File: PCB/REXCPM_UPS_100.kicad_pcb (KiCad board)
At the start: 2 copper layers, 51.3 x 18.3 mm, 14 parts, among them J1 Model_100_System_BUS, J2 SM04B, U1 2G02

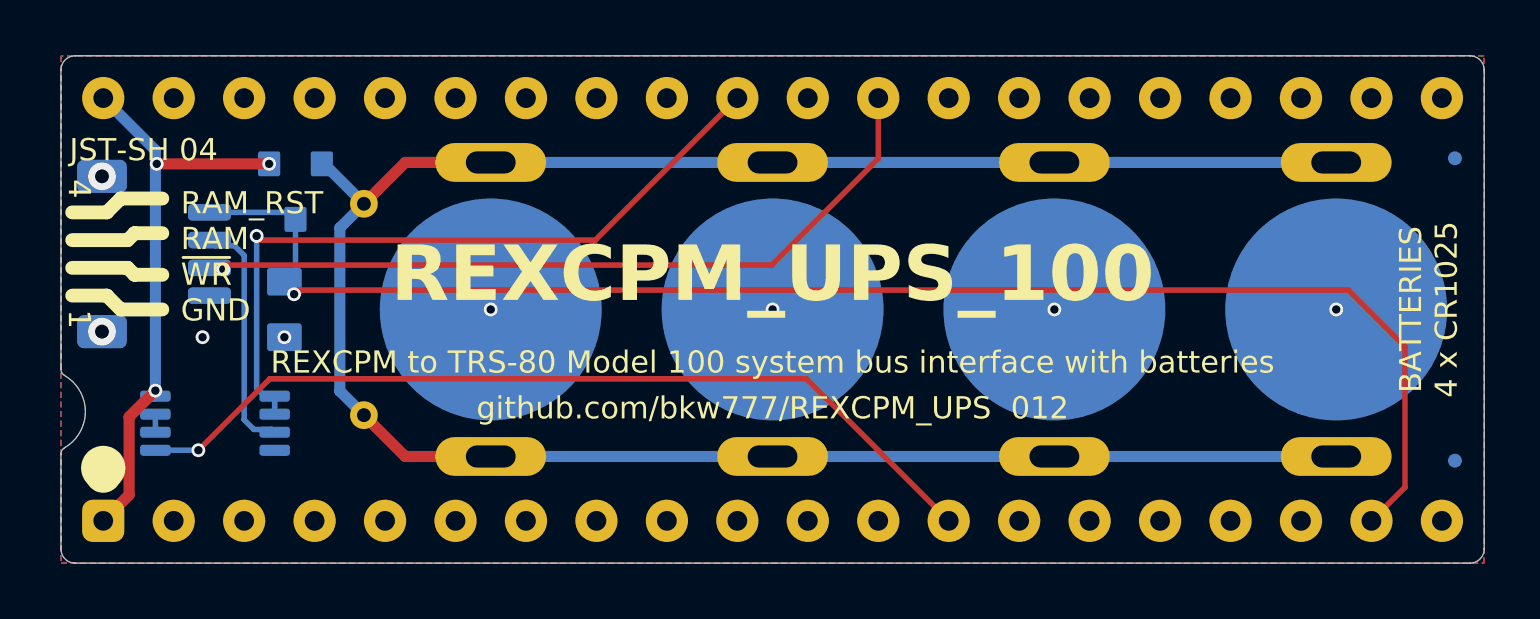
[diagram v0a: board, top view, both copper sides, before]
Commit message: move 1u cap from RAMRST to VBUS
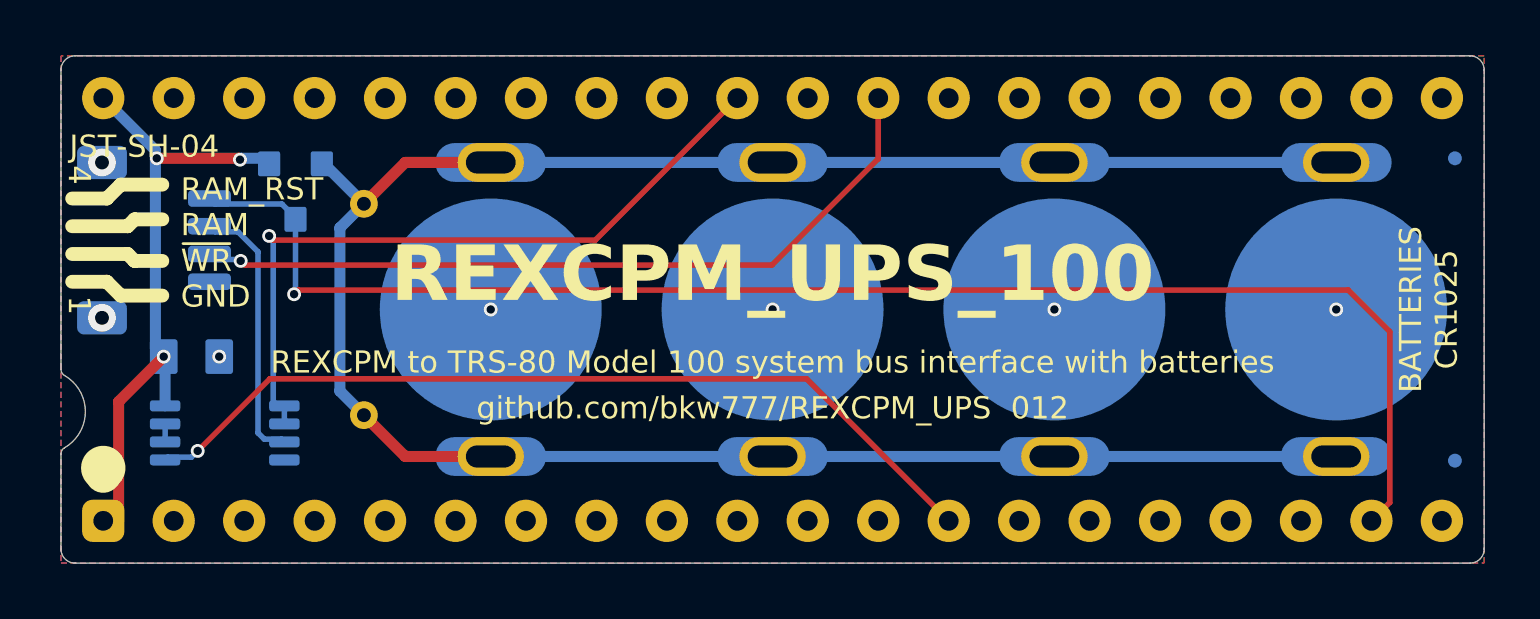
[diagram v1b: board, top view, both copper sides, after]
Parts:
- moved C1 3.76 mm to (115.6, 106.5), turned to 0 degrees
- moved J2 0.50 mm to (114.2, 102.3)
- moved U1 0.49 mm to (116.8, 109.2)
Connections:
- C1 pad 1: /RAM_RST -> VBUS
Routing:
- net VBUS: track 21.1 -> 23.4 mm
- net /RAM: track 8.69 -> 9.74 mm
- net /RAM_RST: track 54.0 -> 53.4 mm
- net GND: vias 8 -> 7
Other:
- board text added: "BATTERIES CR1025"
- board text added: "JST-SH-04"
- board text removed: "BATTERIES 4 x CR1025"
- board text removed: "JST-SH 04"
